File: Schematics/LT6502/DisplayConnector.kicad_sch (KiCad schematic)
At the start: 7 parts, among them J5 Conn_02x20_Odd_Even, U8 TXB0108PW, U9 TXB0108PW

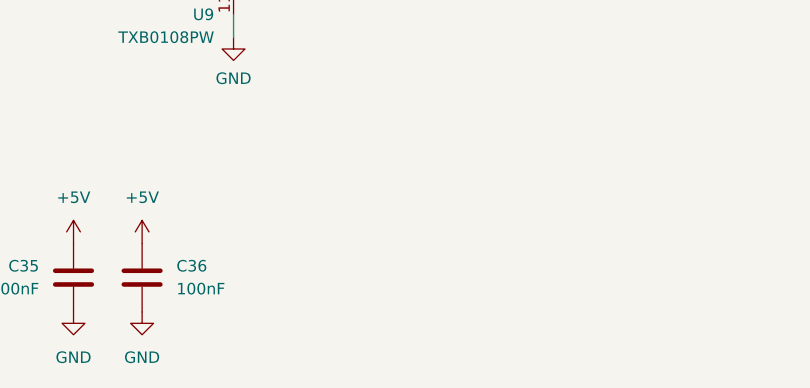
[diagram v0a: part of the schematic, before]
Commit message: Further work on Schematics, All parts placed on PCB
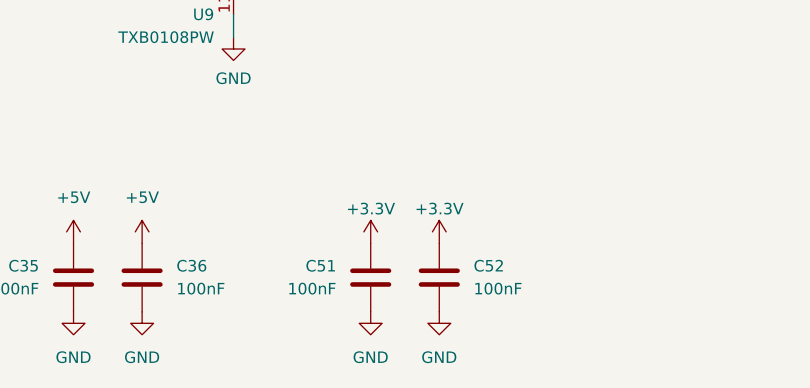
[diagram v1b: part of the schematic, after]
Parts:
- added C51, C52: 100nF, Capacitor_SMD:C_0603_1608Metric, symbol Device:C
- R67, R68: footprint Resistor_SMD:R_0603_1608Metric_Pad0.98x0.95mm_HandSolder -> Resistor_SMD:R_0402_1005Metric
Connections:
- net +3.3V: now also C51.1, C52.1
- net GND: now also C51.2, C52.2

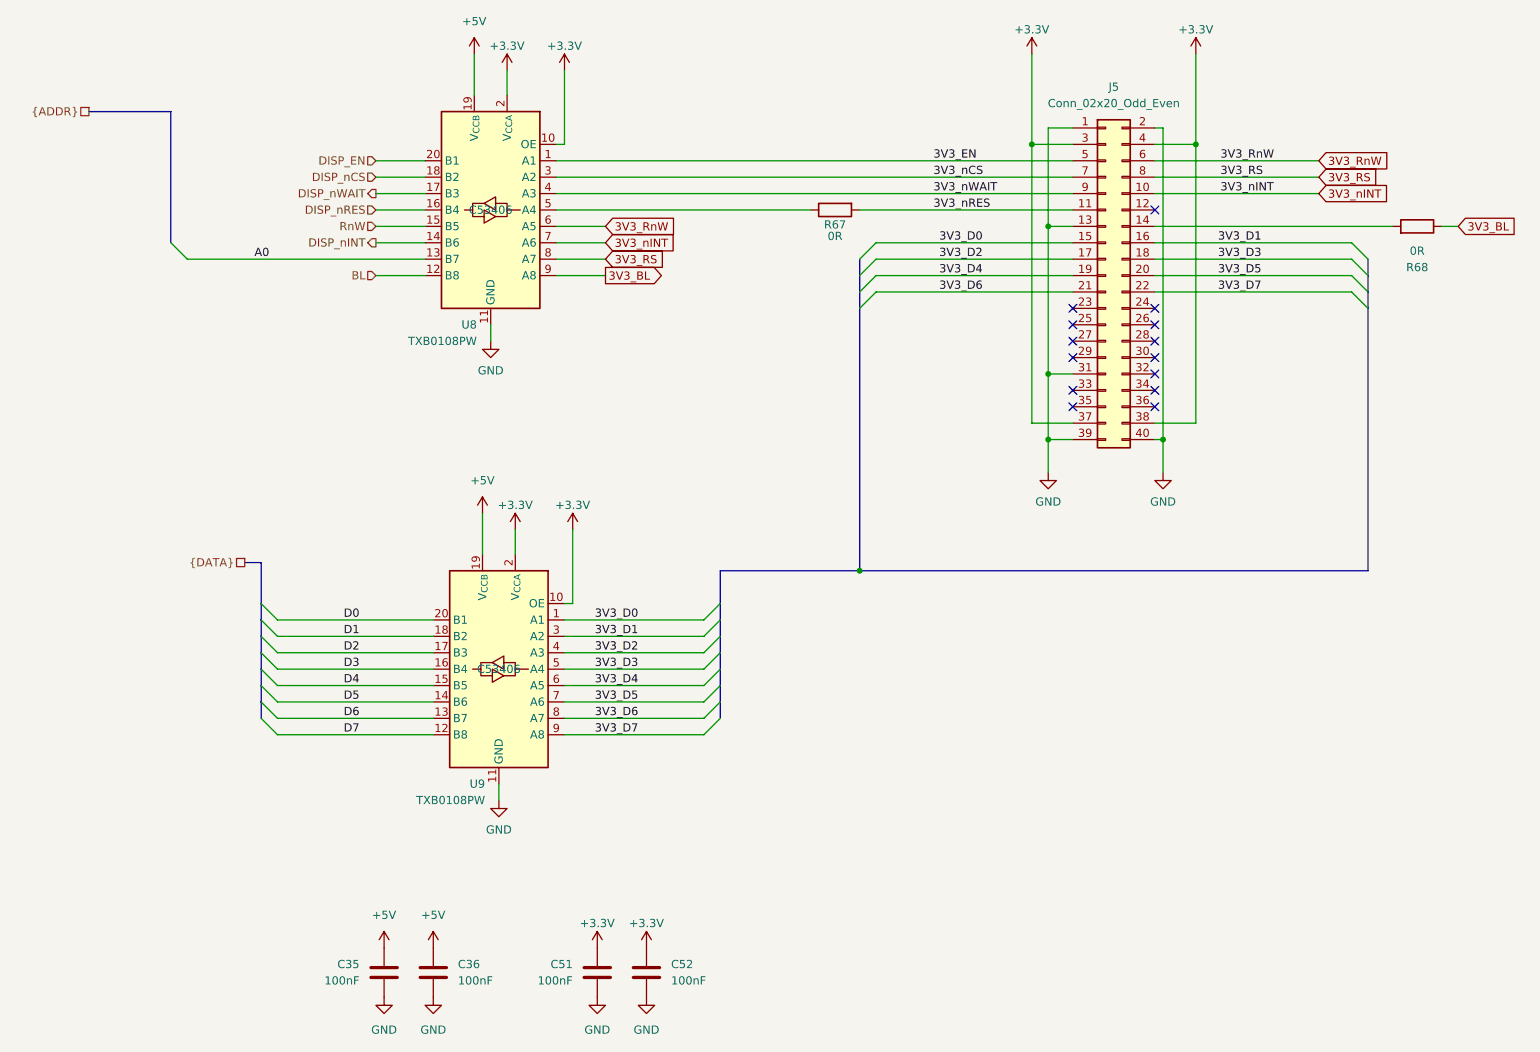
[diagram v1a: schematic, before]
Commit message: Updated main board and started keybed
main board a bit wider due to keybed width
created keybed, begun routing
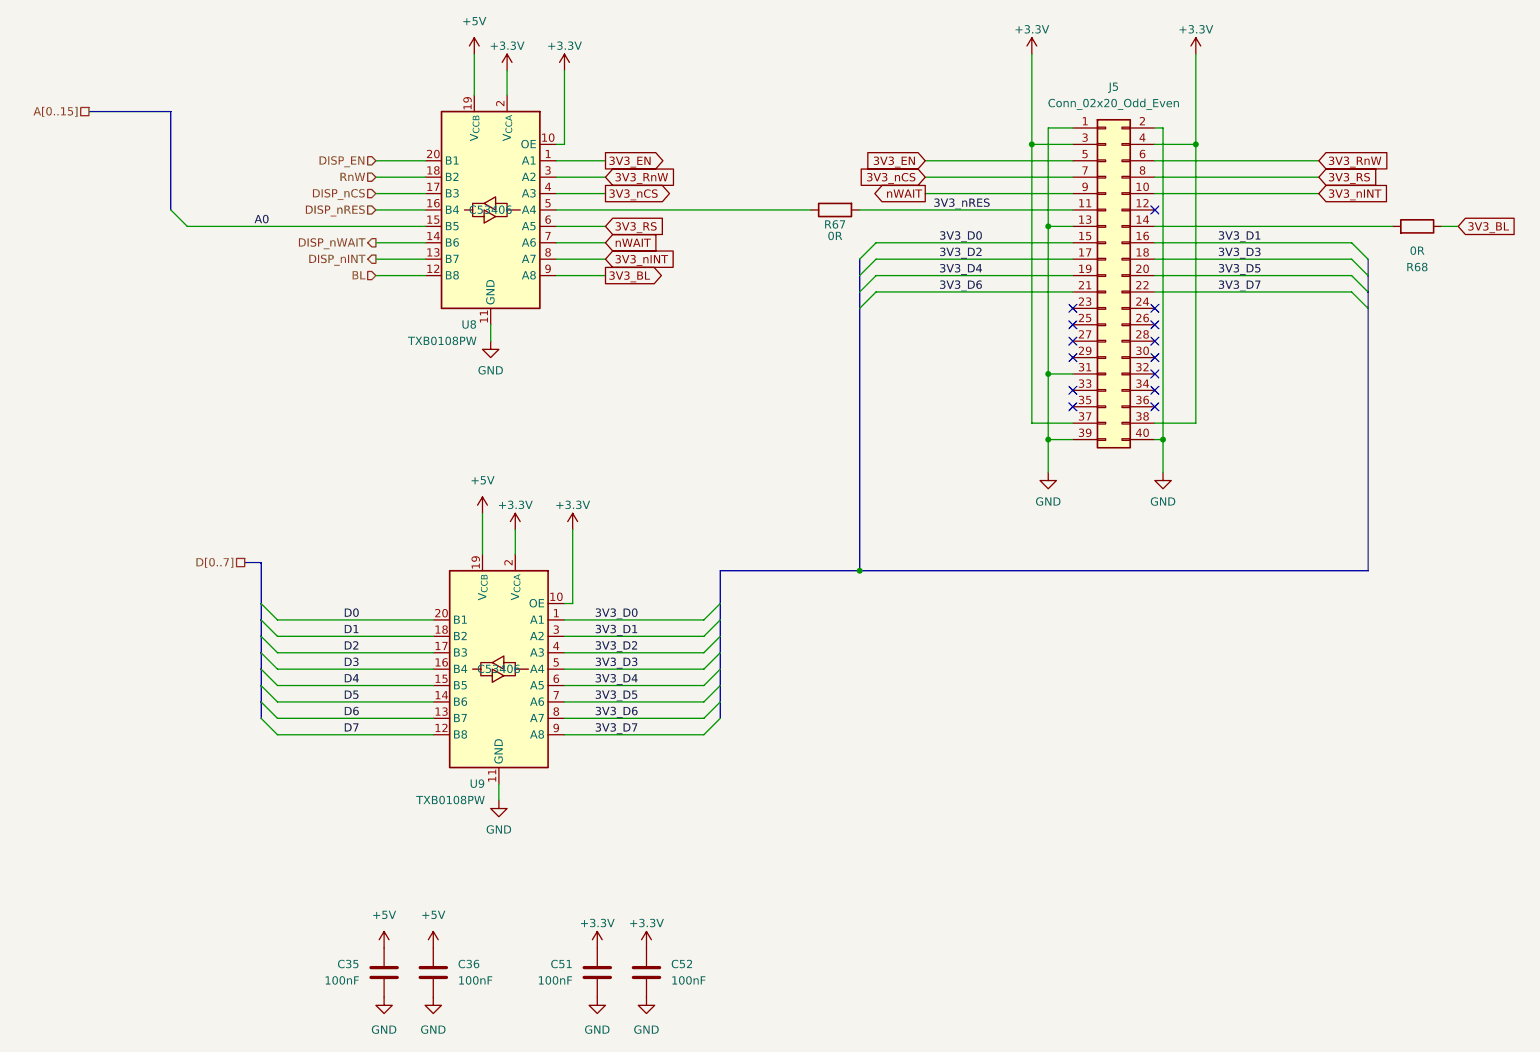
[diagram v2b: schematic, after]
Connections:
- net 3V3_RS: now also U8.6 (A5); no longer U8.8 (A7)
- net 3V3_RnW: now also U8.3 (A2); no longer U8.6 (A5)
- net 3V3_nCS: now also U8.4 (A3); no longer U8.3 (A2)
- net 3V3_nINT: now also U8.8 (A7); no longer U8.7 (A6)
- net A0: now also U8.15 (B5); no longer U8.13 (B7)
- net DISP_nCS: now also U8.17 (B3); no longer U8.18 (B2)
- net DISP_nINT: now also U8.13 (B7); no longer U8.14 (B6)
- net DISP_nWAIT: now also U8.14 (B6); no longer U8.17 (B3)
- net RnW: now also U8.18 (B2); no longer U8.15 (B5)
- net 3V3_nWAIT renamed nWAIT
- net nWAIT: now also U8.7 (A6); no longer U8.4 (A3)

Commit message: Updated BoMs ordered PCBs
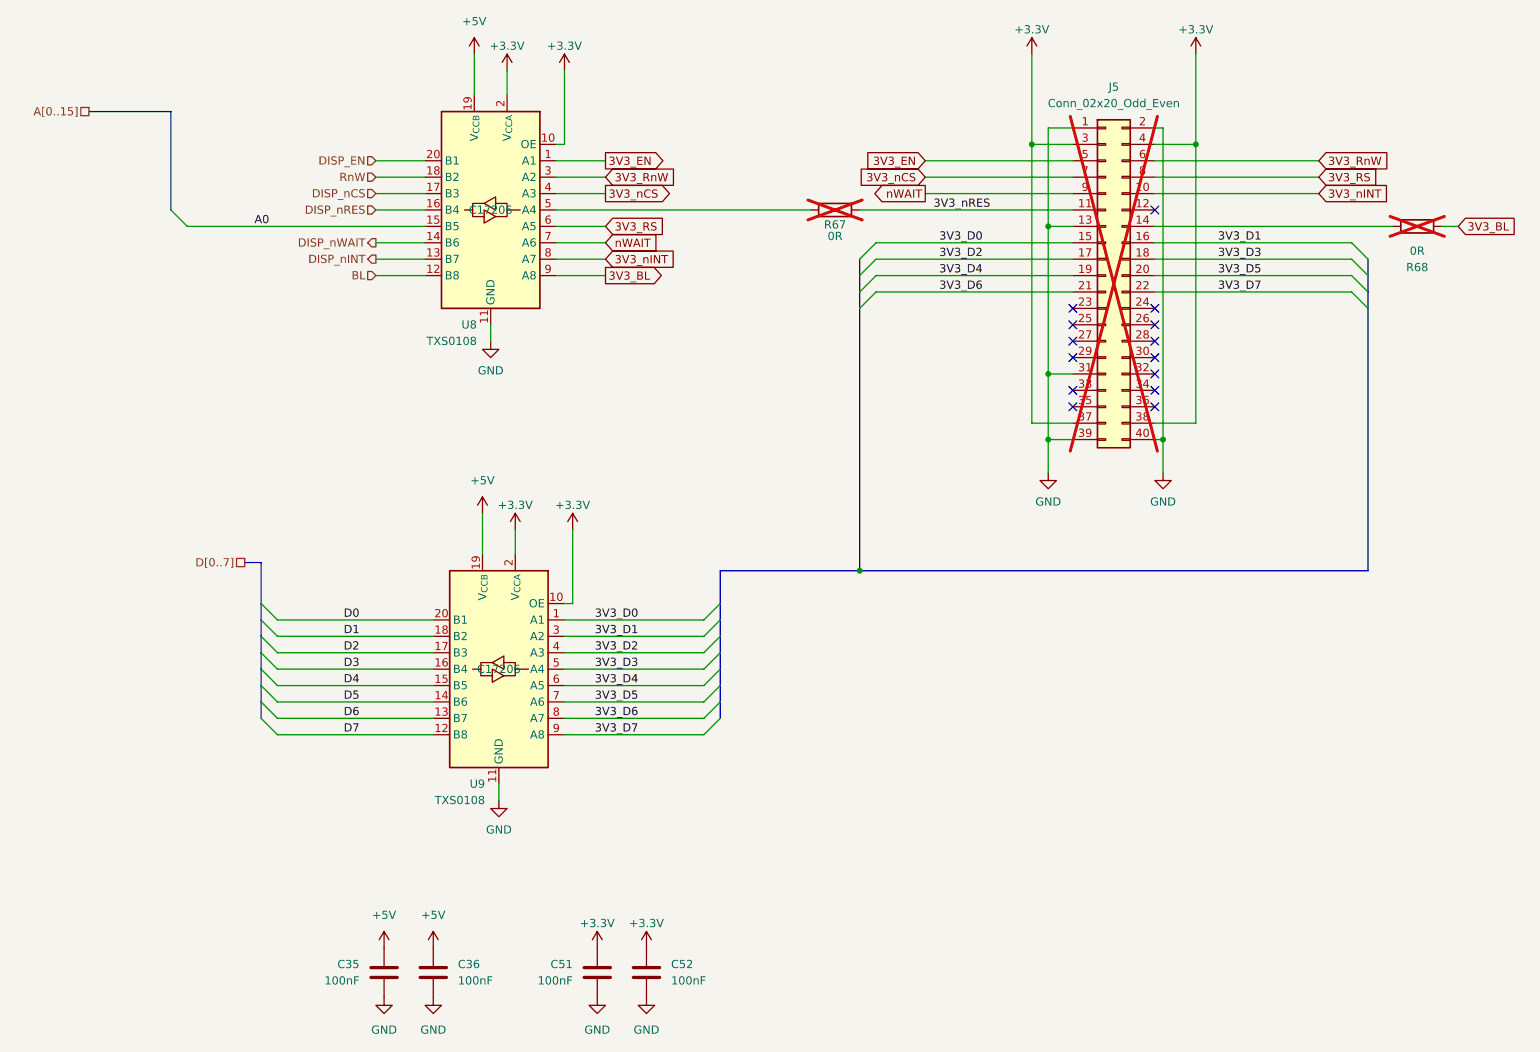
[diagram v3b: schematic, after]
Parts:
- C35, C36, C51, C52: LCSC C49678 -> C113803
- J5: LCSC (none) -> DNF; now not fitted
- R67, R68: now not fitted
- U8, U9: value TXB0108PW -> TXS0108; LCSC C53406 -> C17206
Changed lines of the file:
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@@
 		(in_bom yes)
 		(on_board yes)
-		(dnp no)
+		(dnp yes)
 		(property "Reference" "R67"
 			(at 151.13 63.246 90)
@@
 			)
 		)
-		(property "LCSC" "C49678"
+		(property "LCSC" "C113803"
 			(at 88.9 179.07 0)
 			(effects
@@
 		(in_bom yes)
 		(on_board yes)
-		(dnp no)
+		(dnp yes)
 		(fields_autoplaced yes)
 		(property "Reference" "J5"
@@
 		)
 		(property "Description" "Generic connector, double row, 02x20, odd/even pin numbering scheme (row 1 odd numbers, row 2 even numbers), script generated (kicad-library-utils/schlib/autogen/connector/)"
+			(at 193.04 71.12 0)
+			(effects
+				(font
+					(size 1.27 1.27)
+				)
+				(hide yes)
+			)
+		)
+		(property "LCSC" "DNF"
 			(at 193.04 71.12 0)
 			(effects
@@
 			)
 		)
-		(property "LCSC" "C49678"
+		(property "LCSC" "C113803"
 			(at 81.28 179.07 0)
 			(effects
@@
 			)
 		)
-		(property "Value" "TXB0108PW"
+		(property "Value" "TXS0108"
 			(at 96.9167 152.4 0)
 			(effects
@@
 			)
 		)
-		(property "LCSC" "C53406"
+		(property "LCSC" "C17206"
 			(at 99.06 132.08 0)
 			(effects
@@
 			)
 		)
-		(property "Value" "TXB0108PW"
+		(property "Value" "TXS0108"
 			(at 95.6467 81.28 0)
 			(effects
@@
 			)
 		)
-		(property "LCSC" "C53406"
+		(property "LCSC" "C17206"
 			(at 97.79 60.96 0)
 			(effects
@@
 			)
 		)
-		(property "LCSC" "C49678"
+		(property "LCSC" "C113803"
 			(at 121.92 179.07 0)
 			(effects
@@
 		(in_bom yes)
 		(on_board yes)
-		(dnp no)
+		(dnp yes)
 		(property "Reference" "R68"
 			(at 241.3 69.85 90)
@@
 			)
 		)
-		(property "LCSC" "C49678"
+		(property "LCSC" "C113803"
 			(at 114.3 179.07 0)
 			(effects

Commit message: Auto stash before merge of "main" and "origin/main"
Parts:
- J5, R67: now fitted
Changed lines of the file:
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@@
 		(in_bom yes)
 		(on_board yes)
-		(dnp yes)
+		(dnp no)
 		(property "Reference" "R67"
 			(at 151.13 63.246 90)
@@
 		(in_bom yes)
 		(on_board yes)
-		(dnp yes)
+		(dnp no)
 		(fields_autoplaced yes)
 		(property "Reference" "J5"

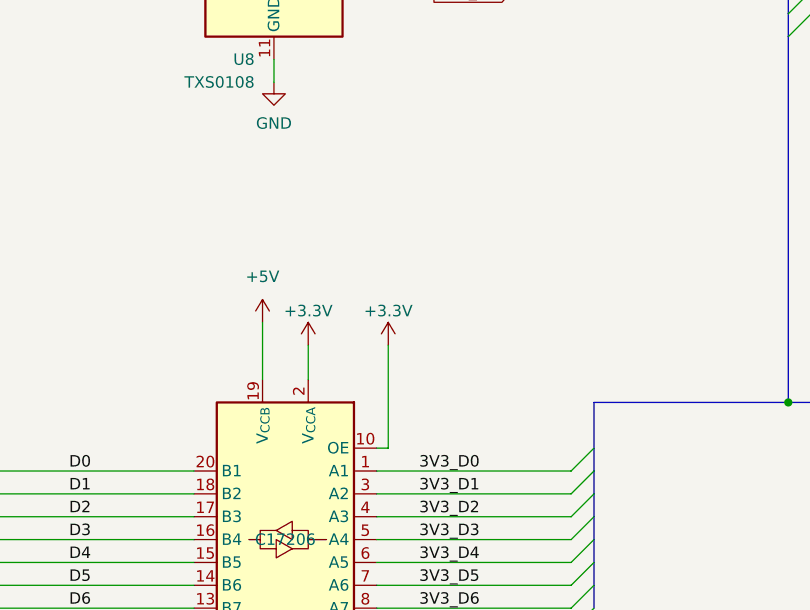
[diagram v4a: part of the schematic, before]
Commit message: Added enable for TXS0108 on data bus
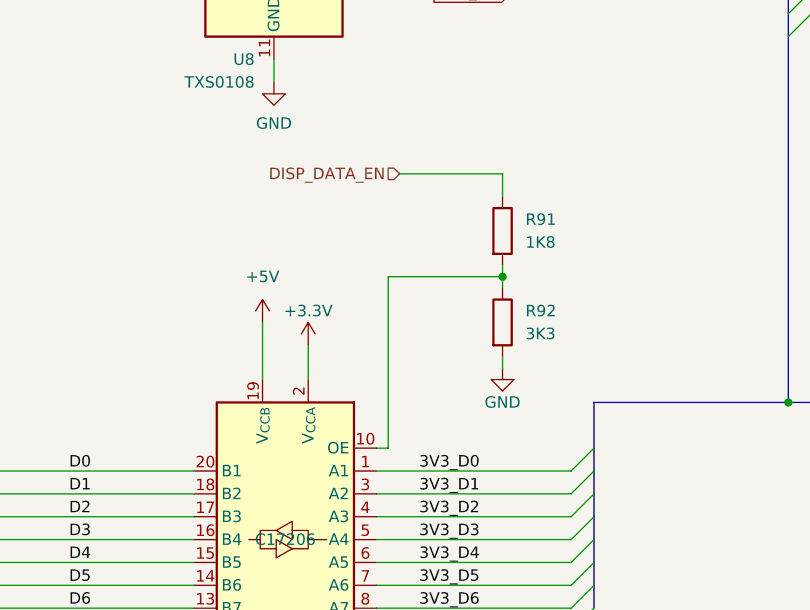
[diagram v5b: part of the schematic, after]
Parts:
- added R91: 1K8, Resistor_SMD:R_0603_1608Metric, symbol Device:R
- added R92: 3K3, Resistor_SMD:R_0603_1608Metric, symbol Device:R
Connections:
- net +3.3V: no longer U9.10 (OE)
- net GND: now also R92.2
- new net: R91.2, R92.1, U9.10 (OE)
- new net DISP_DATA_EN: R91.1

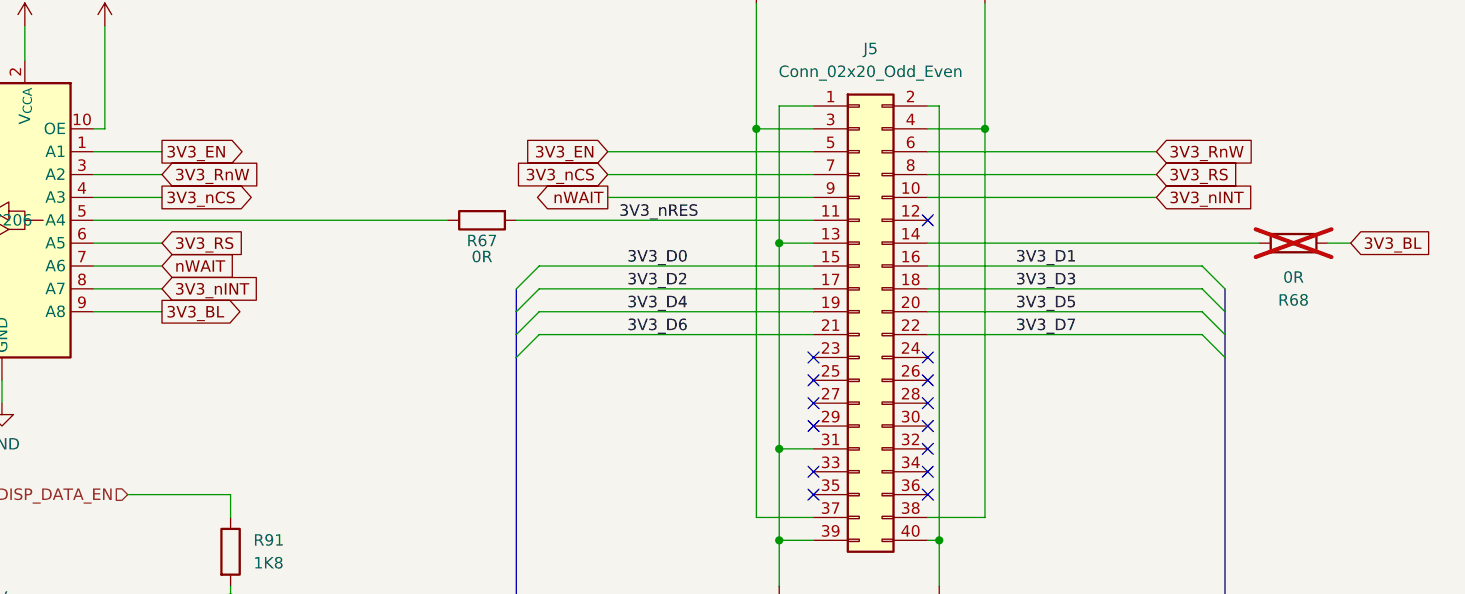
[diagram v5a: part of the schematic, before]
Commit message: PCB/Schematic edits
moved speaker hole a little
made nRES resistor for display no fit (this upsets them for some reason)
Added diodes to ensure USB Console chip is powered when nothing attached (this causes issues with booting.
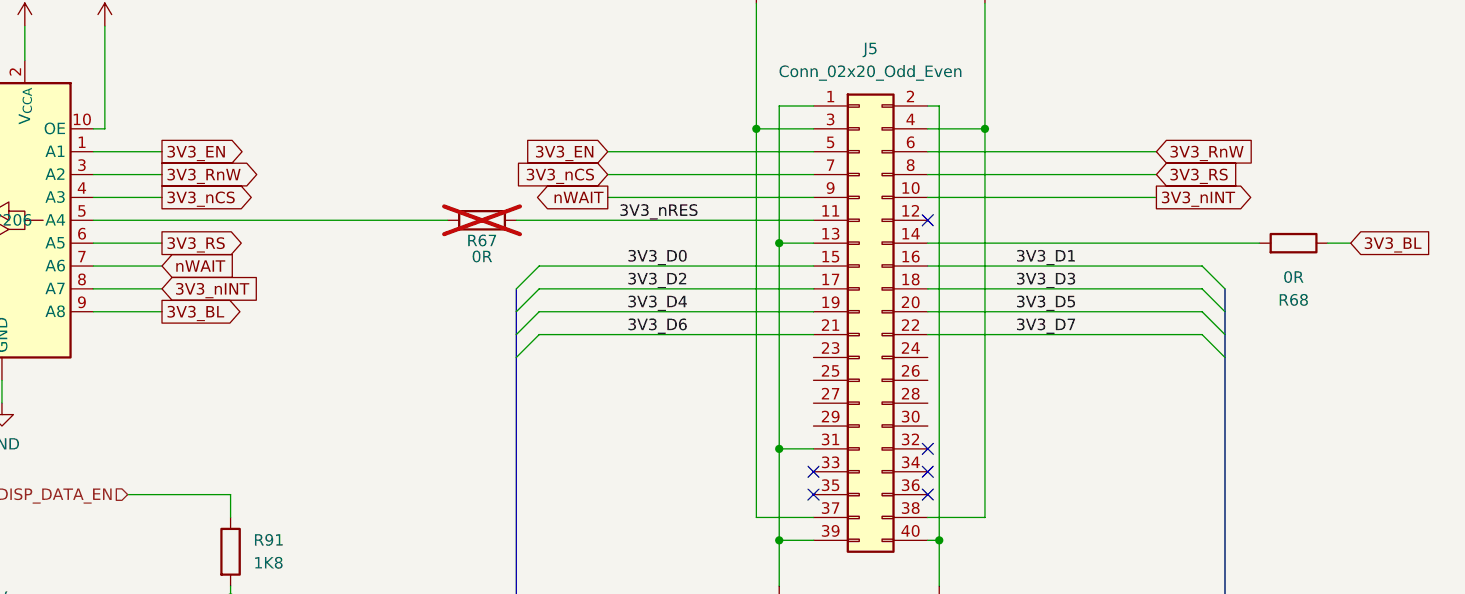
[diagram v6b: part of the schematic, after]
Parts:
- R67: now not fitted
- R68: now fitted
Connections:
- no-connect marks 14 -> 6
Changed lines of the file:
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@@
 	)
 	(no_connect
-		(at 200.66 83.82)
-	)
-	(no_connect
-		(at 200.66 78.74)
-	)
-	(no_connect
-		(at 200.66 81.28)
-	)
-	(no_connect
-		(at 187.96 83.82)
-	)
-	(no_connect
-		(at 187.96 78.74)
-	)
-	(no_connect
-		(at 187.96 76.2)
-	)
-	(no_connect
-		(at 200.66 76.2)
-	)
-	(no_connect
-		(at 187.96 81.28)
-	)
-	(no_connect
 		(at 200.66 60.96)
 	)
@@
 	)
 	(global_label "3V3_RS"
-		(shape input)
+		(shape output)
 		(at 115.57 63.5 0)
 		(fields_autoplaced yes)
@@
 	)
 	(global_label "3V3_RnW"
-		(shape input)
+		(shape output)
 		(at 115.57 55.88 0)
 		(fields_autoplaced yes)
@@
 	)
 	(global_label "3V3_nINT"
-		(shape input)
+		(shape output)
 		(at 226.06 58.42 0)
 		(fields_autoplaced yes)
@@
 		(in_bom yes)
 		(on_board yes)
-		(dnp no)
+		(dnp yes)
 		(property "Reference" "R67"
 			(at 151.13 63.246 90)
@@
 		(in_bom yes)
 		(on_board yes)
-		(dnp yes)
+		(dnp no)
 		(property "Reference" "R68"
 			(at 241.3 69.85 90)
